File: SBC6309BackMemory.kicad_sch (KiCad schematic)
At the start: 11 parts, among them J3 Conn_01x16, J4 Conn_01x08, J5 Conn_01x08, J6 Conn_01x04, J7 Conn_01x08, J8 Conn_01x06, J9 Conn_01x08

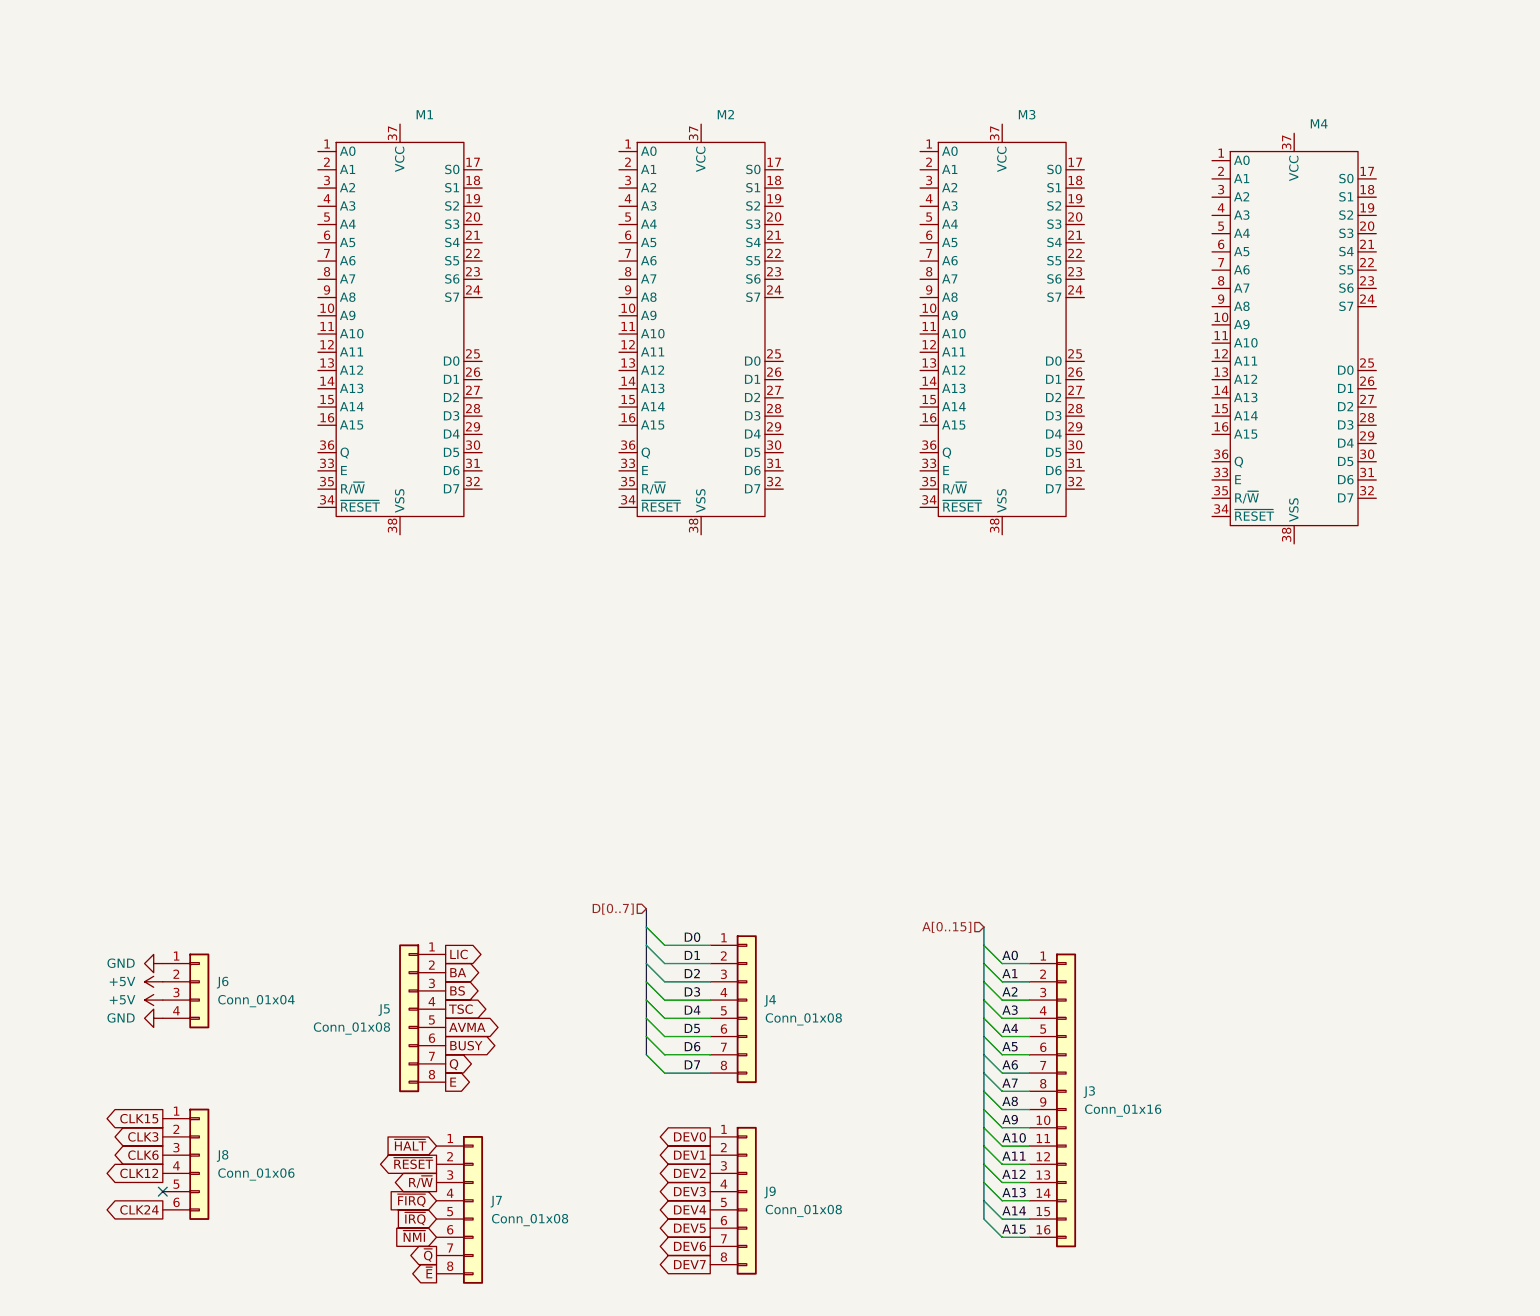
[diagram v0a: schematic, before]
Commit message: route primary functional traces
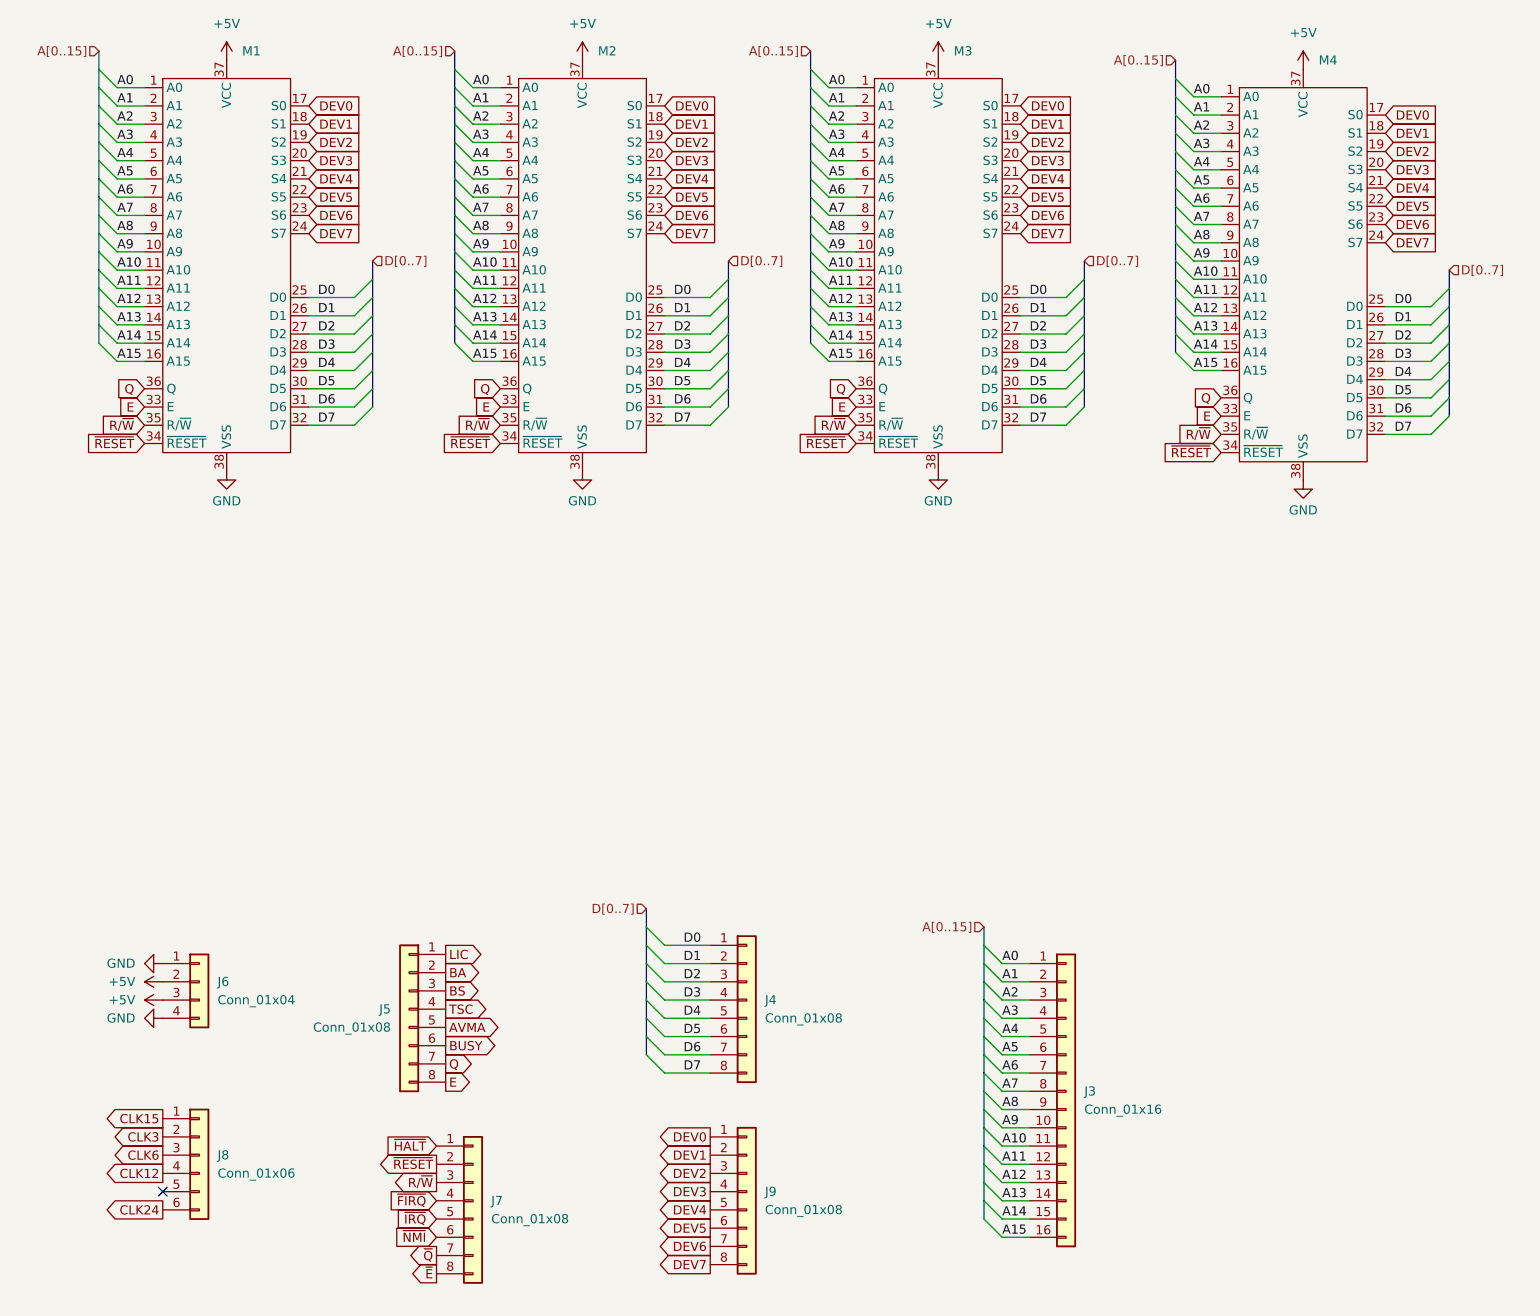
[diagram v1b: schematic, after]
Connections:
- net +5V: now also M1.37 (VCC), M2.37 (VCC), M3.37 (VCC), M4.37 (VCC)
- net A0: now also M1.1 (A0), M2.1 (A0), M3.1 (A0), M4.1 (A0)
- net A1: now also M1.2 (A1), M2.2 (A1), M3.2 (A1), M4.2 (A1)
- net A10: now also M1.11 (A10), M2.11 (A10), M3.11 (A10), M4.11 (A10)
- net A11: now also M1.12 (A11), M2.12 (A11), M3.12 (A11), M4.12 (A11)
- net A12: now also M1.13 (A12), M2.13 (A12), M3.13 (A12), M4.13 (A12)
- net A13: now also M1.14 (A13), M2.14 (A13), M3.14 (A13), M4.14 (A13)
- net A14: now also M1.15 (A14), M2.15 (A14), M3.15 (A14), M4.15 (A14)
- net A15: now also M1.16 (A15), M2.16 (A15), M3.16 (A15), M4.16 (A15)
- net A2: now also M1.3 (A2), M2.3 (A2), M3.3 (A2), M4.3 (A2)
- net A3: now also M1.4 (A3), M2.4 (A3), M3.4 (A3), M4.4 (A3)
- net A4: now also M1.5 (A4), M2.5 (A4), M3.5 (A4), M4.5 (A4)
- net A5: now also M1.6 (A5), M2.6 (A5), M3.6 (A5), M4.6 (A5)
- net A6: now also M1.7 (A6), M2.7 (A6), M3.7 (A6), M4.7 (A6)
- net A7: now also M1.8 (A7), M2.8 (A7), M3.8 (A7), M4.8 (A7)
- net A8: now also M1.9 (A8), M2.9 (A8), M3.9 (A8), M4.9 (A8)
- net A9: now also M1.10 (A9), M2.10 (A9), M3.10 (A9), M4.10 (A9)
- net D0: now also M1.25 (D0), M2.25 (D0), M3.25 (D0), M4.25 (D0)
- net D1: now also M1.26 (D1), M2.26 (D1), M3.26 (D1), M4.26 (D1)
- net D2: now also M1.27 (D2), M2.27 (D2), M3.27 (D2), M4.27 (D2)
- net D3: now also M1.28 (D3), M2.28 (D3), M3.28 (D3), M4.28 (D3)
- net D4: now also M1.29 (D4), M2.29 (D4), M3.29 (D4), M4.29 (D4)
- net D5: now also M1.30 (D5), M2.30 (D5), M3.30 (D5), M4.30 (D5)
- net D6: now also M1.31 (D6), M2.31 (D6), M3.31 (D6), M4.31 (D6)
- net D7: now also M1.32 (D7), M2.32 (D7), M3.32 (D7), M4.32 (D7)
- net DEV0: now also M1.17 (S0), M2.17 (S0), M3.17 (S0), M4.17 (S0)
- net DEV1: now also M1.18 (S1), M2.18 (S1), M3.18 (S1), M4.18 (S1)
- net DEV2: now also M1.19 (S2), M2.19 (S2), M3.19 (S2), M4.19 (S2)
- net DEV3: now also M1.20 (S3), M2.20 (S3), M3.20 (S3), M4.20 (S3)
- net DEV4: now also M1.21 (S4), M2.21 (S4), M3.21 (S4), M4.21 (S4)
- net DEV5: now also M1.22 (S5), M2.22 (S5), M3.22 (S5), M4.22 (S5)
- net DEV6: now also M1.23 (S6), M2.23 (S6), M3.23 (S6), M4.23 (S6)
- net DEV7: now also M1.24 (S7), M2.24 (S7), M3.24 (S7), M4.24 (S7)
- net E: now also M1.33 (E), M2.33 (E), M3.33 (E), M4.33 (E)
- net GND: now also M1.38 (VSS), M2.38 (VSS), M3.38 (VSS), M4.38 (VSS)
- net Q: now also M1.36 (Q), M2.36 (Q), M3.36 (Q), M4.36 (Q)
- net R/~{W}: now also M1.35 (R/~{W}), M2.35 (R/~{W}), M3.35 (R/~{W}), M4.35 (R/~{W})
- net ~{RESET}: now also M1.34 (~{RESET}), M2.34 (~{RESET}), M3.34 (~{RESET}), M4.34 (~{RESET})
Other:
- moved on the sheet: M1, M2, M3, M4

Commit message: add pass through connections
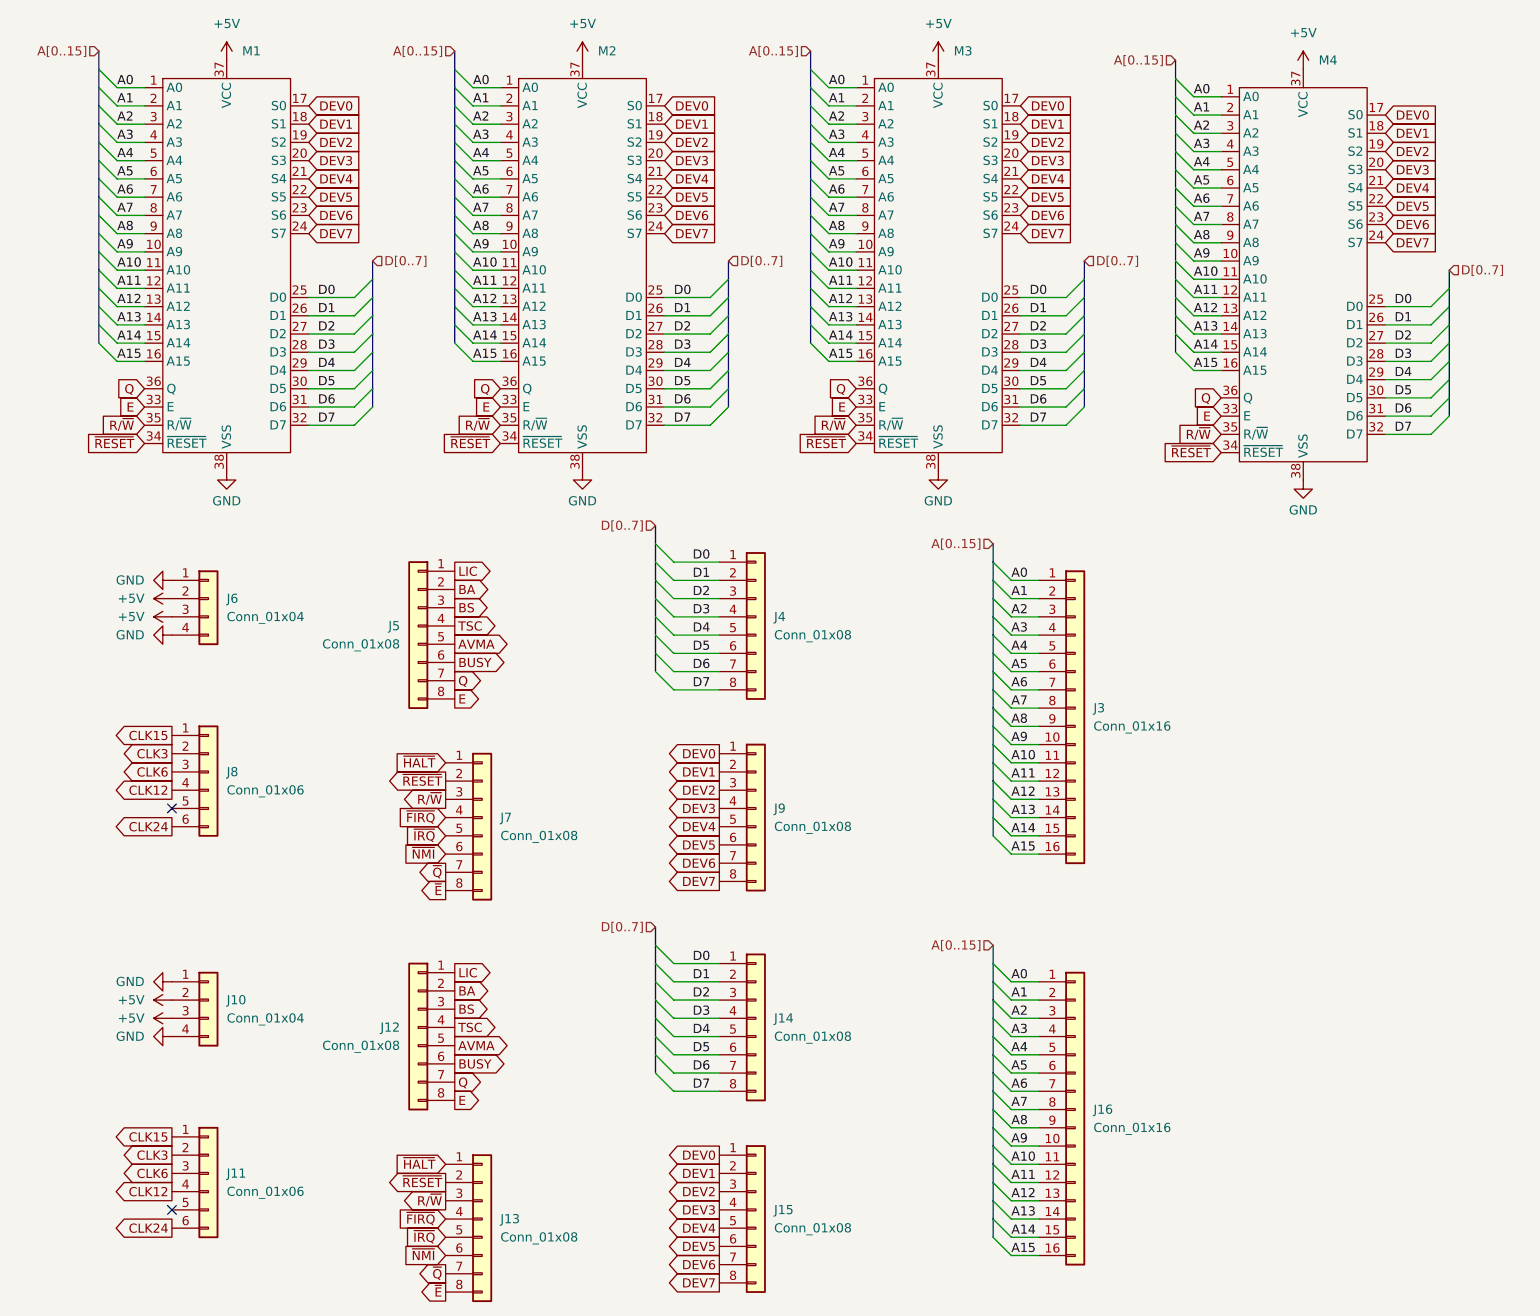
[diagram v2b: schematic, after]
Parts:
- added J10: Conn_01x04, Connector_PinHeader_2.54mm:PinHeader_1x04_P2.54mm_Vertical, symbol Connector_Generic:Conn_01x04
- added J11: Conn_01x06, Connector_PinHeader_2.54mm:PinHeader_1x06_P2.54mm_Vertical, symbol Connector_Generic:Conn_01x06
- added J12, J13, J14, J15: Conn_01x08, Connector_PinHeader_2.54mm:PinHeader_1x08_P2.54mm_Vertical, symbol Connector_Generic:Conn_01x08
- added J16: Conn_01x16, Connector_PinHeader_2.54mm:PinHeader_1x16_P2.54mm_Vertical, symbol Connector_Generic:Conn_01x16
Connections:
- net +5V: now also J10.2 (Pin_2), J10.3 (Pin_3)
- net A0: now also J16.1 (Pin_1)
- net A1: now also J16.2 (Pin_2)
- net A10: now also J16.11 (Pin_11)
- net A11: now also J16.12 (Pin_12)
- net A12: now also J16.13 (Pin_13)
- net A13: now also J16.14 (Pin_14)
- net A14: now also J16.15 (Pin_15)
- net A15: now also J16.16 (Pin_16)
- net A2: now also J16.3 (Pin_3)
- net A3: now also J16.4 (Pin_4)
- net A4: now also J16.5 (Pin_5)
- net A5: now also J16.6 (Pin_6)
- net A6: now also J16.7 (Pin_7)
- net A7: now also J16.8 (Pin_8)
- net A8: now also J16.9 (Pin_9)
- net A9: now also J16.10 (Pin_10)
- net AVMA: now also J12.5 (Pin_5)
- net BA: now also J12.2 (Pin_2)
- net BS: now also J12.3 (Pin_3)
- net BUSY: now also J12.6 (Pin_6)
- net CLK12: now also J11.4 (Pin_4)
- net CLK15: now also J11.1 (Pin_1)
- net CLK24: now also J11.6 (Pin_6)
- net CLK3: now also J11.2 (Pin_2)
- net CLK6: now also J11.3 (Pin_3)
- net D0: now also J14.1 (Pin_1)
- net D1: now also J14.2 (Pin_2)
- net D2: now also J14.3 (Pin_3)
- net D3: now also J14.4 (Pin_4)
- net D4: now also J14.5 (Pin_5)
- net D5: now also J14.6 (Pin_6)
- net D6: now also J14.7 (Pin_7)
- net D7: now also J14.8 (Pin_8)
- net DEV0: now also J15.1 (Pin_1)
- net DEV1: now also J15.2 (Pin_2)
- net DEV2: now also J15.3 (Pin_3)
- net DEV3: now also J15.4 (Pin_4)
- net DEV4: now also J15.5 (Pin_5)
- net DEV5: now also J15.6 (Pin_6)
- net DEV6: now also J15.7 (Pin_7)
- net DEV7: now also J15.8 (Pin_8)
- net E: now also J12.8 (Pin_8)
- net GND: now also J10.1 (Pin_1), J10.4 (Pin_4)
- net LIC: now also J12.1 (Pin_1)
- net Q: now also J12.7 (Pin_7)
- net R/~{W}: now also J13.3 (Pin_3)
- net TSC: now also J12.4 (Pin_4)
- net ~{E}: now also J13.8 (Pin_8)
- net ~{FIRQ}: now also J13.4 (Pin_4)
- net ~{HALT}: now also J13.1 (Pin_1)
- net ~{IRQ}: now also J13.5 (Pin_5)
- net ~{NMI}: now also J13.6 (Pin_6)
- net ~{Q}: now also J13.7 (Pin_7)
- net ~{RESET}: now also J13.2 (Pin_2)
- no-connect marks 1 -> 2
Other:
- moved on the sheet: J3, J4, J5, J6, J7, J8, J9

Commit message: finish routing
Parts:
- removed J11: Conn_01x06, Connector_PinHeader_2.54mm:PinHeader_1x06_P2.54mm_Vertical, symbol Connector_Generic:Conn_01x06
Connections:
- net ~{E}: no longer J13.8 (Pin_8)
- net ~{Q}: no longer J13.7 (Pin_7)
- no-connect marks 2 -> 3
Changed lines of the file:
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@@
 	(paper "A4")
 	(no_connect
+		(at 73.66 190.5)
+	)
+	(no_connect
 		(at 35.56 125.73)
 	)
 	(no_connect
-		(at 35.56 181.61)
+		(at 73.66 193.04)
 	)
 	(bus_entry
@@
 		)
 	)
-	(global_label "~{E}"
-		(shape output)
-		(at 73.66 193.04 180)
-		(fields_autoplaced yes)
-		(effects
-			(font
-				(size 1.27 1.27)
-			)
-			(justify right)
-		)
-		(property "Intersheetrefs" "${INTERSHEET_REFS}"
-			(at 69.5258 193.04 0)
-			(effects
-				(font
-					(size 1.27 1.27)
-				)
-				(justify right)
-				(hide yes)
-			)
-		)
-	)
 	(global_label "DEV5"
 		(shape input)
@@
 		)
 	)
-	(global_label "CLK15"
-		(shape output)
-		(at 35.56 171.45 180)
-		(fields_autoplaced yes)
-		(effects
-			(font
-				(size 1.27 1.27)
-			)
-			(justify right)
-		)
-		(property "Intersheetrefs" "${INTERSHEET_REFS}"
-			(at 26.5877 171.45 0)
-			(effects
-				(font
-					(size 1.27 1.27)
-				)
-				(justify right)
-				(hide yes)
-			)
-		)
-	)
 	(global_label "CLK3"
 		(shape output)
@@
 		)
 	)
-	(global_label "CLK3"
-		(shape output)
-		(at 35.56 173.99 180)
-		(fields_autoplaced yes)
-		(effects
-			(font
-				(size 1.27 1.27)
-			)
-			(justify right)
-		)
-		(property "Intersheetrefs" "${INTERSHEET_REFS}"
-			(at 27.7972 173.99 0)
-			(effects
-				(font
-					(size 1.27 1.27)
-				)
-				(justify right)
-				(hide yes)
-			)
-		)
-	)
 	(global_label "E"
 		(shape input)
@@
 		)
 	)
-	(global_label "~{Q}"
-		(shape output)
-		(at 73.66 190.5 180)
-		(fields_autoplaced yes)
-		(effects
-			(font
-				(size 1.27 1.27)
-			)
-			(justify right)
-		)
-		(property "Intersheetrefs" "${INTERSHEET_REFS}"
-			(at 69.3443 190.5 0)
-			(effects
-				(font
-					(size 1.27 1.27)
-				)
-				(justify right)
-				(hide yes)
-			)
-		)
-	)
 	(global_label "R{slash}~{W}"
 		(shape input)
@@
 		)
 	)
-	(global_label "CLK24"
-		(shape output)
-		(at 35.56 184.15 180)
-		(fields_autoplaced yes)
-		(effects
-			(font
-				(size 1.27 1.27)
-			)
-			(justify right)
-		)
-		(property "Intersheetrefs" "${INTERSHEET_REFS}"
-			(at 26.5877 184.15 0)
-			(effects
-				(font
-					(size 1.27 1.27)
-				)
-				(justify right)
-				(hide yes)
-			)
-		)
-	)
 	(global_label "~{FIRQ}"
 		(shape input)
@@
 		)
 	)
-	(global_label "CLK6"
-		(shape output)
-		(at 35.56 176.53 180)
-		(fields_autoplaced yes)
-		(effects
-			(font
-				(size 1.27 1.27)
-			)
-			(justify right)
-		)
-		(property "Intersheetrefs" "${INTERSHEET_REFS}"
-			(at 27.7972 176.53 0)
-			(effects
-				(font
-					(size 1.27 1.27)
-				)
-				(justify right)
-				(hide yes)
-			)
-		)
-	)
 	(global_label "DEV1"
 		(shape input)
@@
 		)
 	)
-	(global_label "CLK12"
-		(shape output)
-		(at 35.56 179.07 180)
-		(fields_autoplaced yes)
-		(effects
-			(font
-				(size 1.27 1.27)
-			)
-			(justify right)
-		)
-		(property "Intersheetrefs" "${INTERSHEET_REFS}"
-			(at 26.5877 179.07 0)
-			(effects
-				(font
-					(size 1.27 1.27)
-				)
-				(justify right)
-				(hide yes)
-			)
-		)
-	)
 	(global_label "E"
 		(shape output)
@@
 					(unit 1)
 				)
-			)
-		)
-	)
-	(symbol
-		(lib_id "Connector_Generic:Conn_01x06")
-		(at 40.64 176.53 0)
-		(unit 1)
-		(exclude_from_sim no)
-		(in_bom yes)
-		(on_board yes)
-		(dnp no)
-		(fields_autoplaced yes)
-		(property "Reference" "J11"
-			(at 43.18 176.5299 0)
-			(effects
-				(font
-					(size 1.27 1.27)
-				)
-				(justify left)
-			)
-		)
-		(property "Value" "Conn_01x06"
-			(at 43.18 179.0699 0)
-			(effects
-				(font
-					(size 1.27 1.27)
-				)
-				(justify left)
-			)
-		)
-		(property "Footprint" "Connector_PinHeader_2.54mm:PinHeader_1x06_P2.54mm_Vertical"
-			(at 40.64 176.53 0)
-			(effects
-				(font
-					(size 1.27 1.27)
-				)
-				(hide yes)
-			)
-		)
-		(property "Datasheet" "~"
-			(at 40.64 176.53 0)
-			(effects
-				(font
-					(size 1.27 1.27)
-				)
-				(hide yes)
-			)
-		)
-		(property "Description" "Generic connector, single row, 01x06, script generated (kicad-library-utils/schlib/autogen/connector/)"
-			(at 40.64 176.53 0)
-			(effects
-				(font
-					(size 1.27 1.27)
-				)
-				(hide yes)
-			)
-		)
-		(pin "2"
-		)
-		(pin "1"
-		)
-		(pin "6"
-		)
-		(pin "3"
-		)
-		(pin "4"
-		)
-		(pin "5"
-		)
-		(instances
-			(project "SBC6309BackMemory"
-				(path "/81a49edd-2a60-4244-9a5d-d95a42388ae8"
-					(reference "J11")
-					(unit 1)
-				)
